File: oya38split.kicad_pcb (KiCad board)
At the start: 2 copper layers, 216.7 x 104.8 mm, 89 parts, among them U1 ProMicro

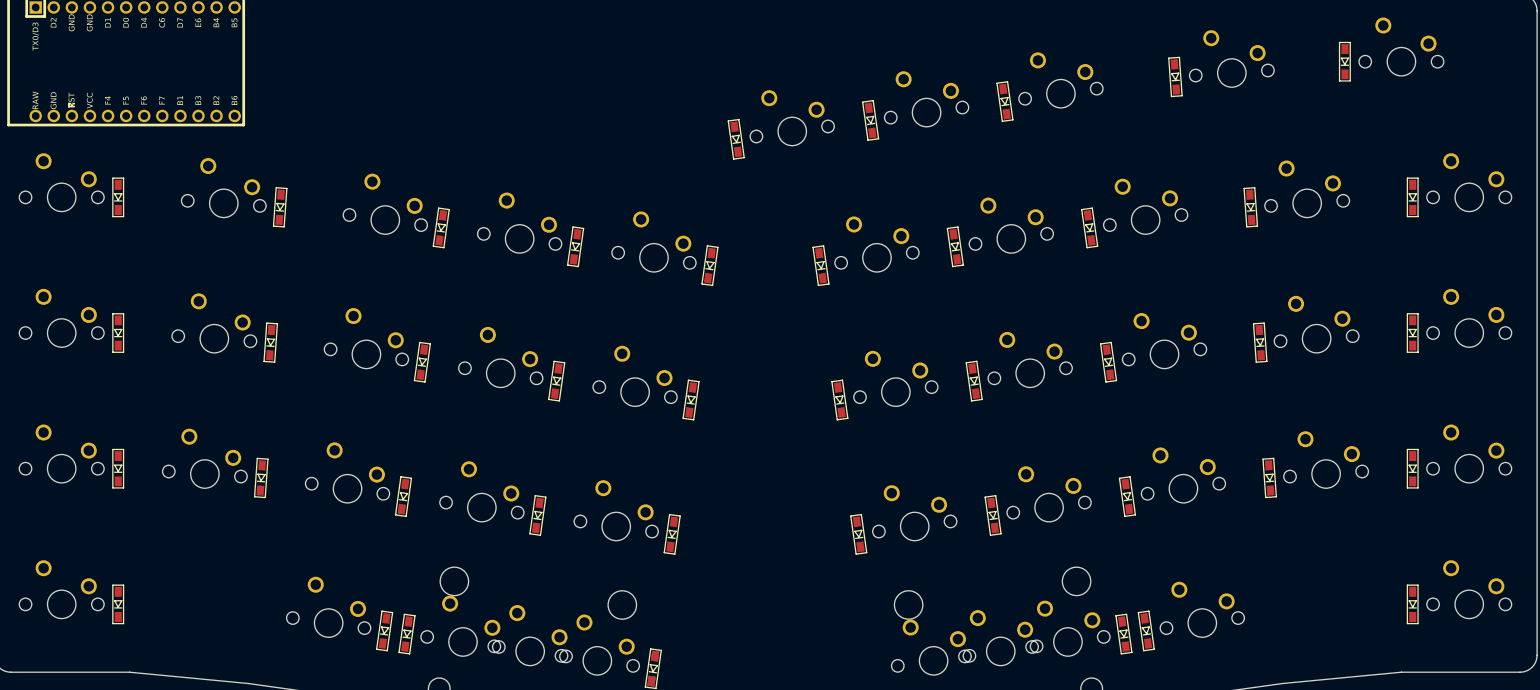
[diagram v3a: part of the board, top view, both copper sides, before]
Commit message: added traces and fixed diode
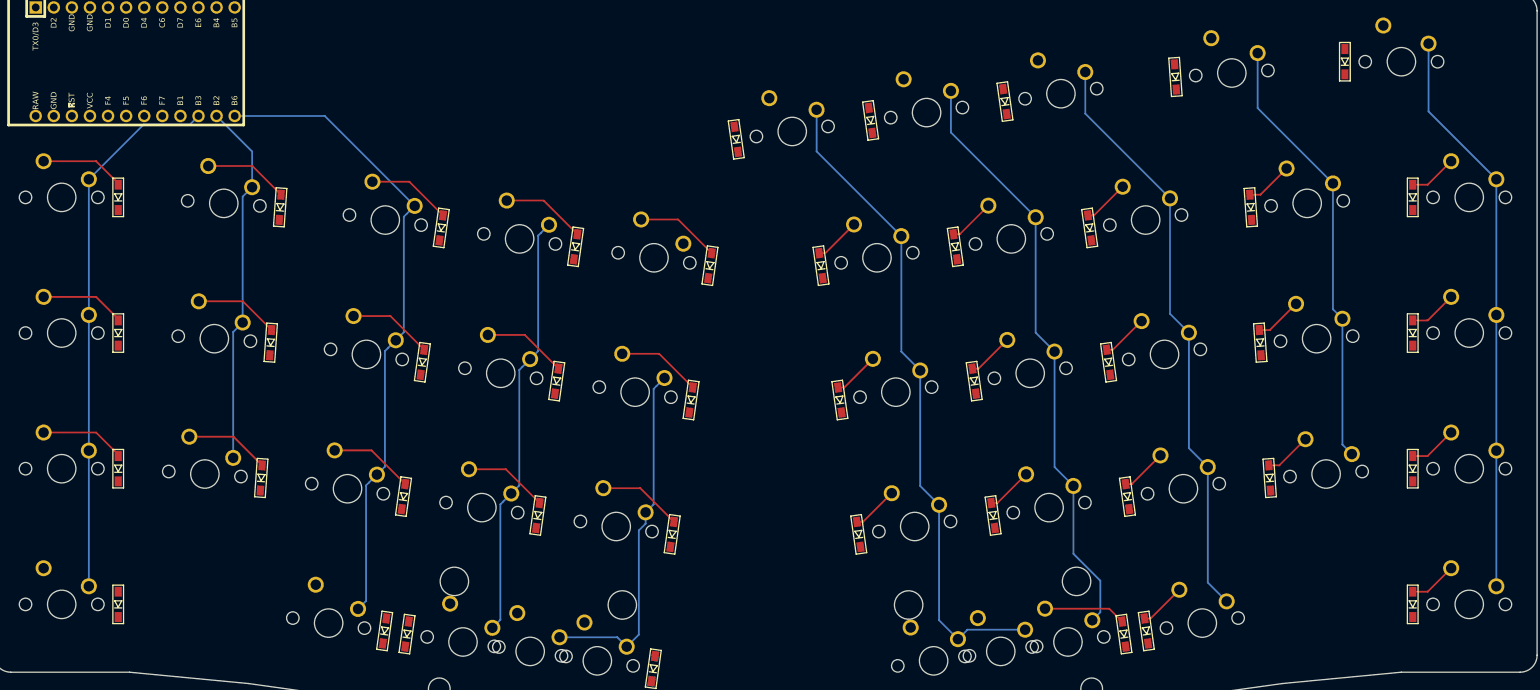
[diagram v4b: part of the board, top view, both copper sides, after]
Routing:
- net col5: track 0.00 -> 92.5 mm
- net col2: track 0.00 -> 90.4 mm
- net col6: track 0.00 -> 83.5 mm
- net col7: track 0.00 -> 82.6 mm
- net col9: track 0.00 -> 80.1 mm
- net col0: track 0.00 -> 76.2 mm
- net col8: track 0.00 -> 61.8 mm
- net col3: track 0.00 -> 59.9 mm
- net col1: track 0.00 -> 51.2 mm
- net col4: track 0.00 -> 49.9 mm
- net Net-(D1-Pad2): track 0.00 -> 12.0 mm
- net Net-(D11-Pad2): track 0.00 -> 12.0 mm
- net Net-(D21-Pad2): track 0.00 -> 12.0 mm
- net Net-(D12-Pad2): track 0.00 -> 11.9 mm
- net Net-(D22-Pad2): track 0.00 -> 11.9 mm
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
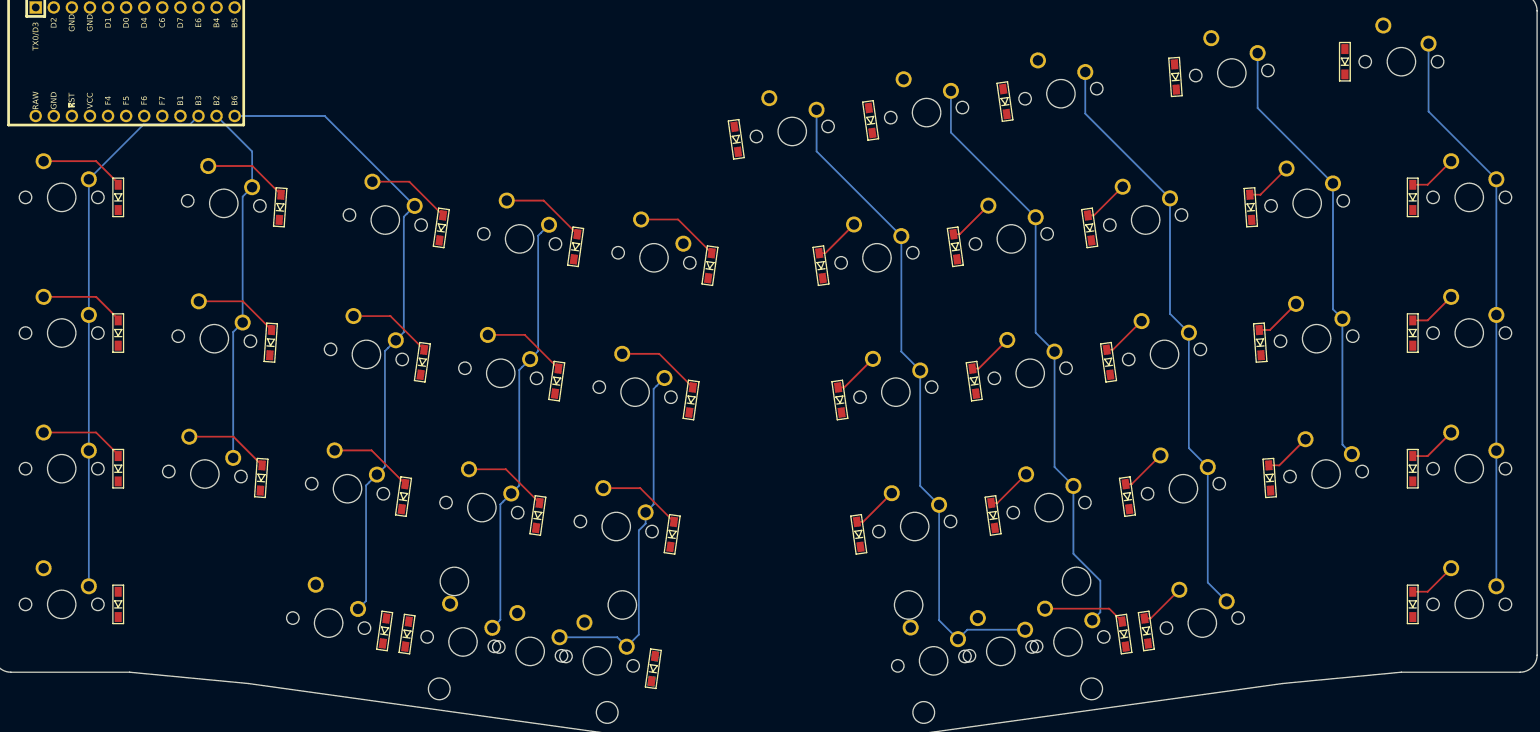
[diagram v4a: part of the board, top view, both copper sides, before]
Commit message: fixed diode placement
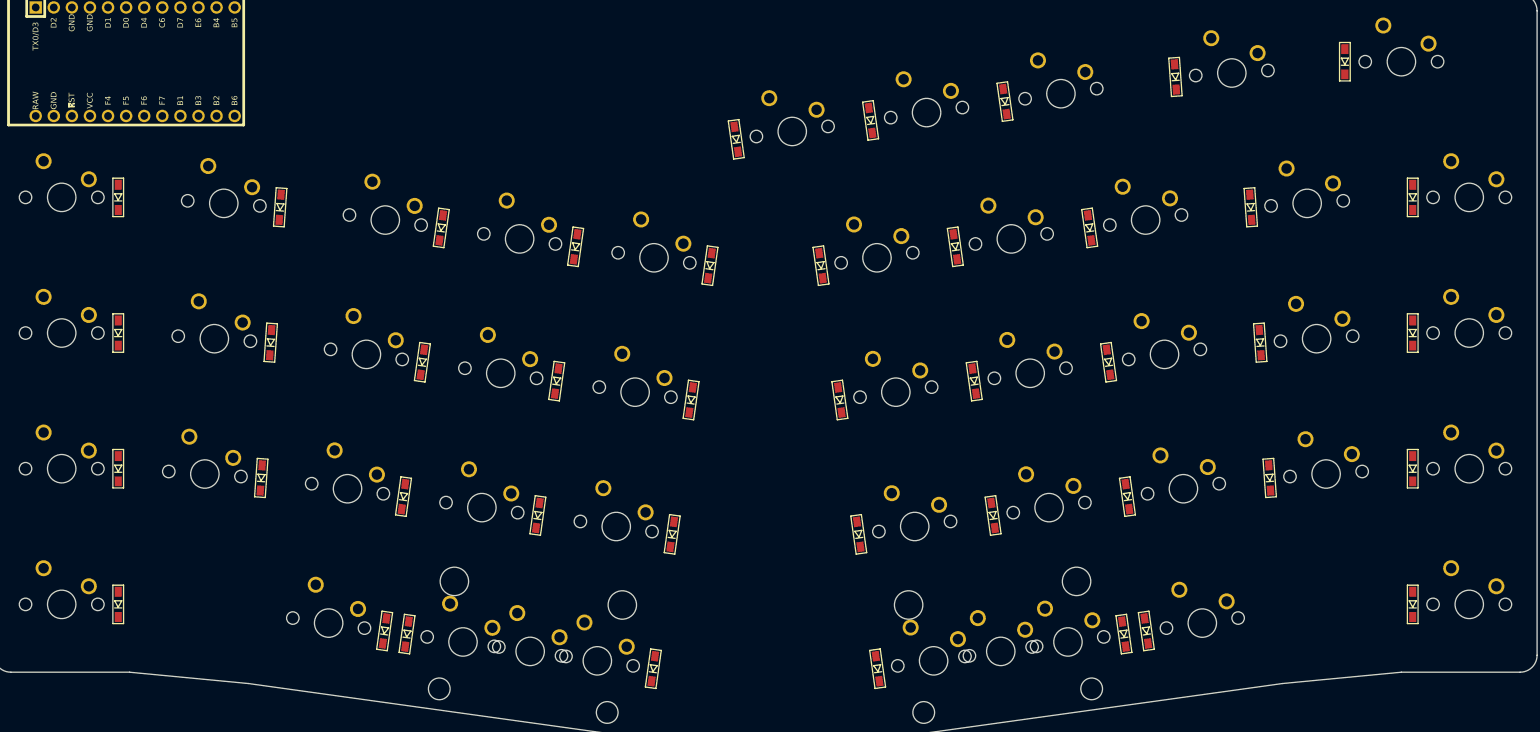
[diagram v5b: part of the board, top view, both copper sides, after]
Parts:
- D35: moved to F.Cu
- moved D35 31.5 mm to (171.7, 123.3), turned to 98 degrees
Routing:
- net col5: track 92.5 -> 0.00 mm
- net col2: track 90.4 -> 0.00 mm
- net col6: track 83.5 -> 0.00 mm
- net col7: track 82.6 -> 0.00 mm
- net col9: track 80.1 -> 0.00 mm
- net col0: track 76.2 -> 0.00 mm
- net col8: track 61.8 -> 0.00 mm
- net col3: track 59.9 -> 0.00 mm
- net col1: track 51.2 -> 0.00 mm
- net col4: track 49.9 -> 0.00 mm
- net Net-(D1-Pad2): track 12.0 -> 0.00 mm
- net Net-(D11-Pad2): track 12.0 -> 0.00 mm
- net Net-(D21-Pad2): track 12.0 -> 0.00 mm
- net Net-(D12-Pad2): track 11.9 -> 0.00 mm
- net Net-(D22-Pad2): track 11.9 -> 0.00 mm
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
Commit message: added traces
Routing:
- net row4: track 0.00 -> 291.8 mm
- net row3: track 0.00 -> 274.3 mm
- net row2: track 0.00 -> 256.7 mm
- net col9: track 0.00 -> 250.8 mm
- net row1: track 0.00 -> 239.2 mm
- net col7: track 0.00 -> 212.4 mm
- net col8: track 0.00 -> 212.2 mm
- net col6: track 0.00 -> 198.1 mm
- net col5: track 0.00 -> 192.0 mm
- net row0: track 0.00 -> 170.1 mm
- net col4: track 0.00 -> 160.9 mm
- net col3: track 0.00 -> 113.5 mm
- net col2: track 0.00 -> 90.4 mm
- net col0: track 0.00 -> 76.2 mm
- net col1: track 0.00 -> 51.2 mm
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
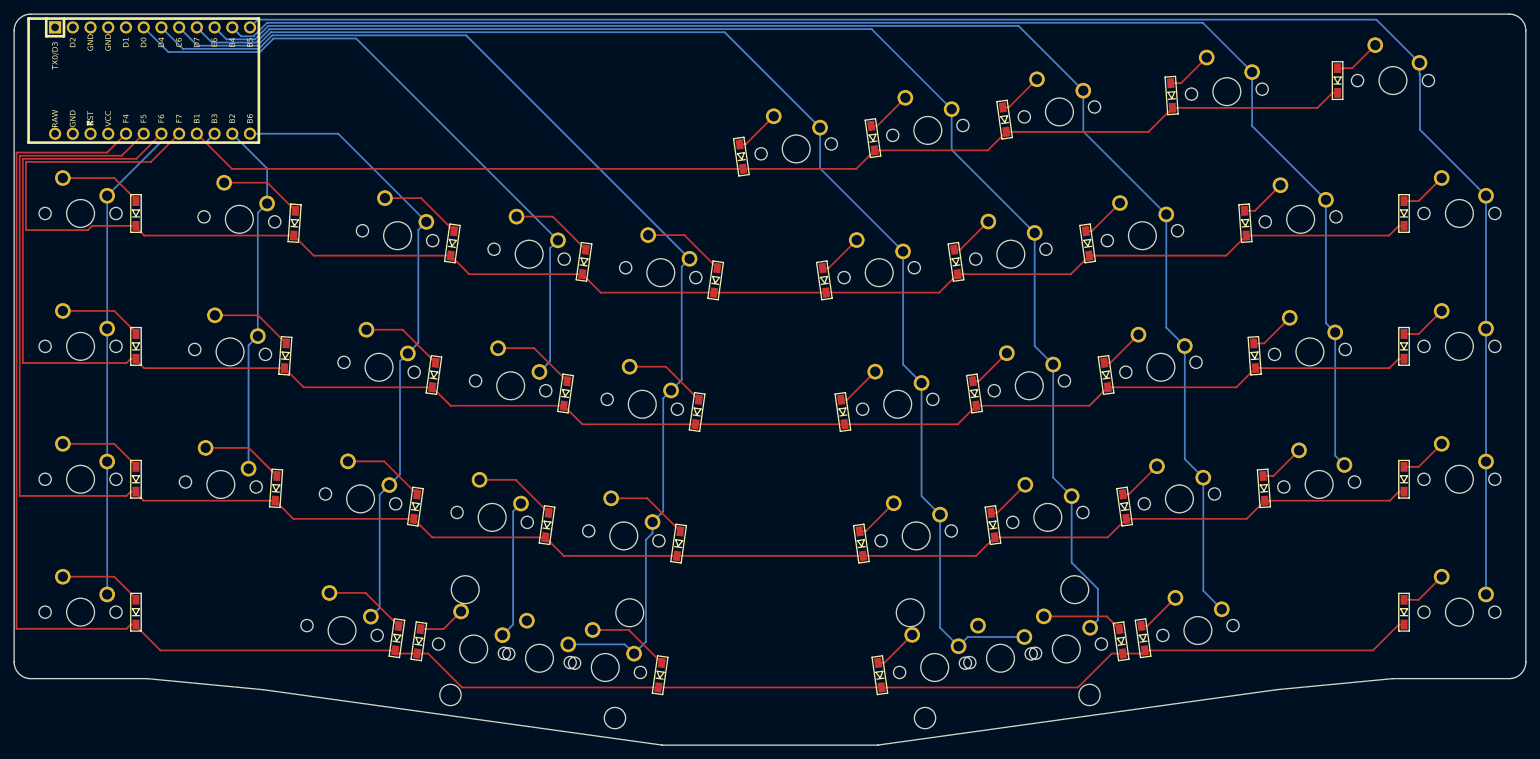
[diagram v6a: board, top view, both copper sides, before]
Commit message: added solder mask and gnd fill
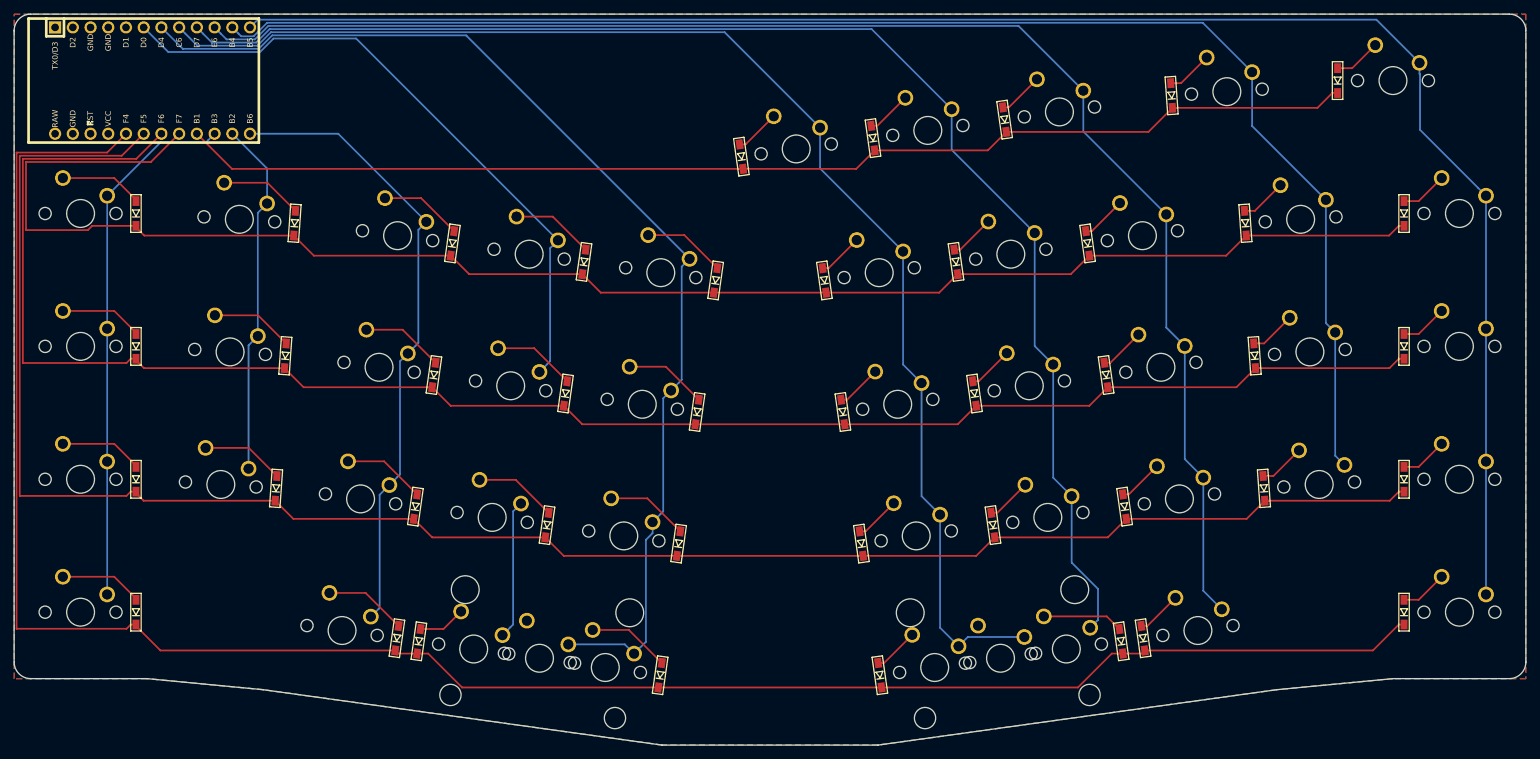
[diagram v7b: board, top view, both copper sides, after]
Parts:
- added G***: LOGO, soldermask:vroyasahi, B.Cu at (159.5, 81.8)
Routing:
- added copper zone on B.Cu, net (none)
- added copper zone on F.Cu, net (none)

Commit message: finalized the first run
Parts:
- G***: moved to F.Cu
- turned G*** to 0 degrees
